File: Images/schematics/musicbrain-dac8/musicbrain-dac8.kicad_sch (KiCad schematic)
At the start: 25 parts, among them J1 BUS, J2 CV OUT, U1 AD5754BREZ, U2 AD5754BREZ, U3 ADR421

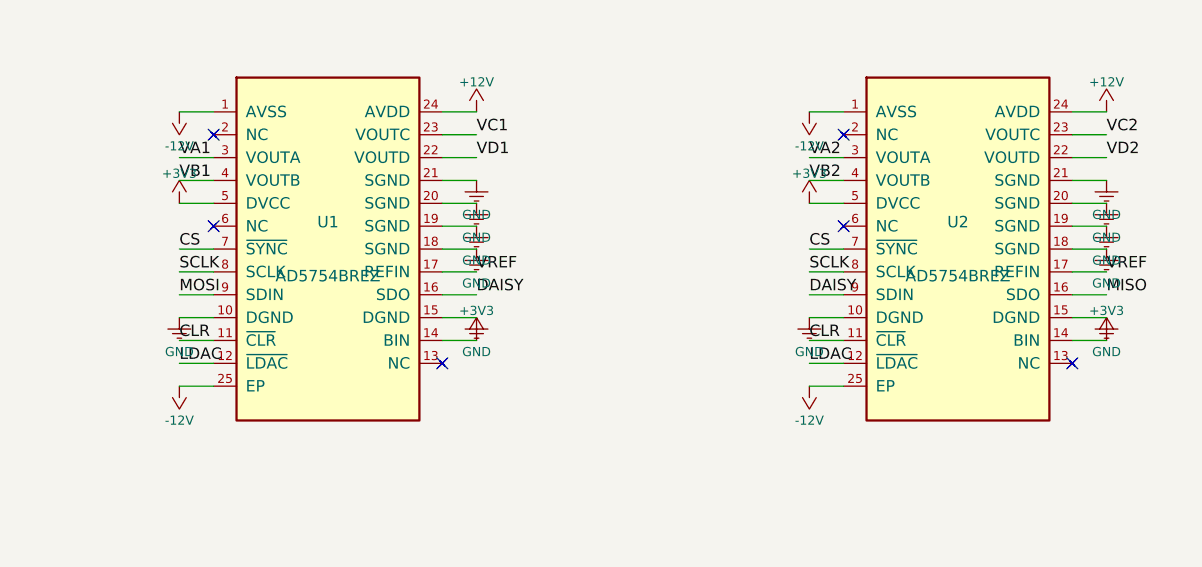
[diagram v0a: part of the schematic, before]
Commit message: DAC8-fix: correcte AD5754-pinout (~LDAC op pin 10, niet 12)
Bij het opzetten van de v2.1-check bleek de "zwevende LDAC" NIET in de
AD5754-breakout te zitten (die matcht Nick's bewezen ontwerp: pin 10 =
~LDAC, al aan GND; pin 12/13 = NC) maar in de deze sessie nieuw gemaakte
DAC8: daar was de AD5754-pinout verhaspeld (LDAC op pin 12 = NC-pad, echte
pin 10 aan GND). Gevolg: de bus-LDAC deed niets en de DAC updatete
transparant i.p.v. sample-synchroon.

- symbool + netmap gecorrigeerd tegen Nick's pinout: 5=BIN(+3V3),
  10=~LDAC(bus), 11=~CLR, 12/13=NC, 14=DVCC(+3V3), 15=DGND(GND)
- LDAC opnieuw geroute naar pin 10 via een trap-entry (CLR 0,6mm
  opgeschoven om ruimte te maken); U2-tak op F.Cu om de CS-B-hop te mijden
- ERC 0, netlijst pad-voor-pad geverifieerd, DRC 0/0; PDF's + fab herzien

De AD5754-breakout blijft ongewijzigd (was al correct).

Co-Authored-By: Claude Fable 5 <noreply@anthropic.com>
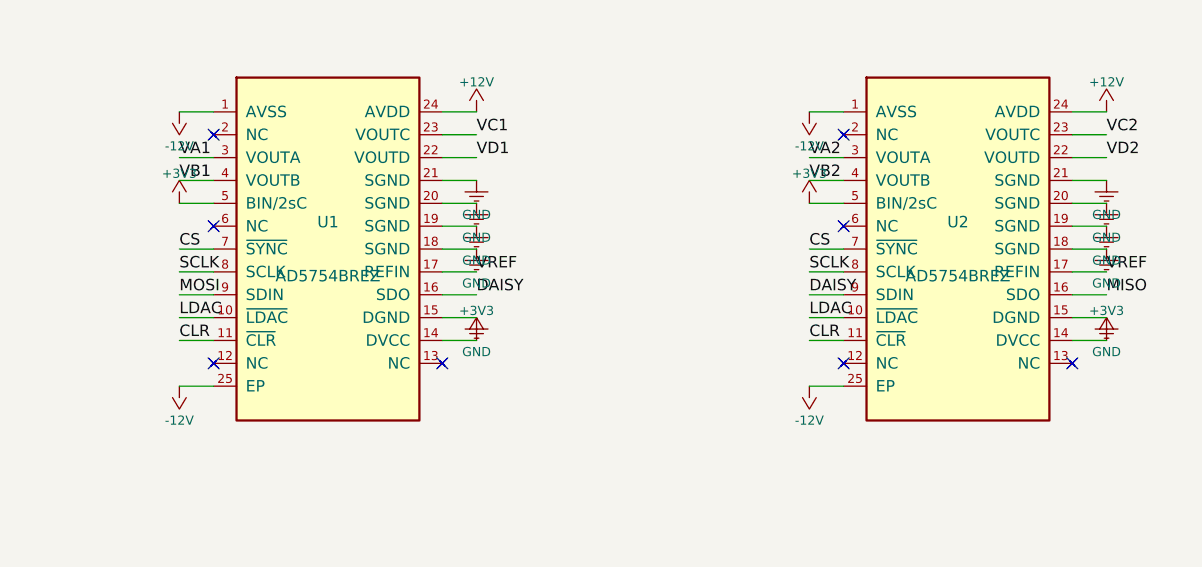
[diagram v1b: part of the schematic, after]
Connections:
- net GND: no longer U1.10 (DGND), U2.10 (DGND)
- net LDAC: now also U1.10 (~{LDAC}), U2.10 (~{LDAC}); no longer U1.12 (~{LDAC}), U2.12 (~{LDAC})
- no-connect marks 11 -> 13

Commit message: DAC8: 10uF bulk op VREF (ADR421-ontkoppeling per datasheet)
Cross-check tegen doc/data-sheets/AD5754BREZ data.md bevestigde de pinout
(3 bronnen) en dat de referentiepen 0,1uF + 10uF hoort te krijgen. C6 was
er al (0,1uF); C14 (10uF, oostrand tussen +12V-spine en C1) toegevoegd op
/VREF naast C6, U1.17, U2.17, U3.8. ERC 0, netcheck OK, DRC 0/0; PDF's +
fab herzien. README: BREZ heeft geen interne ref -> ADR421 verplicht.

Co-Authored-By: Claude Fable 5 <noreply@anthropic.com>
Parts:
- added C14: 10u, Capacitor_SMD:CP_Elec_4x5.3, symbol Device:C_Polarized
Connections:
- net GND: now also C14.2 (-)
- net VREF: now also C14.1 (+)
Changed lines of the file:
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@@
     (instances (project "musicbrain-dac8" (path "/d0900000-0000-4000-8000-000000000000" (reference "#PWR056") (unit 1))))
+  )
+  (symbol (lib_id "Device:C_Polarized") (at 266 190 0)
+    (unit 1) (exclude_from_sim no) (in_bom yes) (on_board yes) (dnp no)
+    (property "Reference" "C14" (at 266 187 0) (effects (font (size 1.27 1.27))))
+    (property "Value" "10u" (at 266 193 0) (effects (font (size 1.27 1.27))))
+    (property "Footprint" "Capacitor_SMD:CP_Elec_4x5.3" (at 266 190 0) (effects (font (size 1.27 1.27)) (hide yes)))
+    (property "Datasheet" "" (at 266 190 0) (effects (font (size 1.27 1.27)) (hide yes)))
+    (instances (project "musicbrain-dac8" (path "/d0900000-0000-4000-8000-000000000000" (reference "C14") (unit 1))))
+  )
+  (wire (pts (xy 266 186.19) (xy 266 184.5)) (stroke (width 0) (type default)))
+  (label "VREF" (at 266 184.5 0) (effects (font (size 1.27 1.27)) (justify left bottom)))
+  (wire (pts (xy 266 193.81) (xy 266 196.17)) (stroke (width 0) (type default)))
+  (symbol (lib_id "power:GND") (at 266 196.17 0)
+    (unit 1) (exclude_from_sim no) (in_bom yes) (on_board yes) (dnp no)
+    (property "Reference" "#PWR057" (at 266 196.17 0) (effects (font (size 1.27 1.27)) (hide yes)))
+    (property "Value" "GND" (at 266 199.98 0) (effects (font (size 1.016 1.016))))
+    (property "Footprint" "" (at 266 196.17 0) (effects (font (size 1.27 1.27)) (hide yes)))
+    (property "Datasheet" "" (at 266 196.17 0) (effects (font (size 1.27 1.27)) (hide yes)))
+    (instances (project "musicbrain-dac8" (path "/d0900000-0000-4000-8000-000000000000" (reference "#PWR057") (unit 1))))
   )
   (wire (pts (xy 300 150) (xy 305.08 150)) (stroke (width 0) (type default)))
   (symbol (lib_id "power:+12V") (at 300 150 0)
     (unit 1) (exclude_from_sim no) (in_bom yes) (on_board yes) (dnp no)
-    (property "Reference" "#PWR057" (at 300 150 0) (effects (font (size 1.27 1.27)) (hide yes)))
+    (property "Reference" "#PWR058" (at 300 150 0) (effects (font (size 1.27 1.27)) (hide yes)))
     (property "Value" "+12V" (at 300 146.698 0) (effects (font (size 1.016 1.016))))
     (property "Footprint" "" (at 300 150 0) (effects (font (size 1.27 1.27)) (hide yes)))
     (property "Datasheet" "" (at 300 150 0) (effects (font (size 1.27 1.27)) (hide yes)))
-    (instances (project "musicbrain-dac8" (path "/d0900000-0000-4000-8000-000000000000" (reference "#PWR057") (unit 1))))
+    (instances (project "musicbrain-dac8" (path "/d0900000-0000-4000-8000-000000000000" (reference "#PWR058") (unit 1))))
   )
   (symbol (lib_id "power:PWR_FLAG") (at 305.08 150 0)
@@
   (symbol (lib_id "power:-12V") (at 314 150 0)
     (unit 1) (exclude_from_sim no) (in_bom yes) (on_board yes) (dnp no)
-    (property "Reference" "#PWR058" (at 314 150 0) (effects (font (size 1.27 1.27)) (hide yes)))
+    (property "Reference" "#PWR059" (at 314 150 0) (effects (font (size 1.27 1.27)) (hide yes)))
     (property "Value" "-12V" (at 314 153.81 0) (effects (font (size 1.016 1.016))))
     (property "Footprint" "" (at 314 150 0) (effects (font (size 1.27 1.27)) (hide yes)))
     (property "Datasheet" "" (at 314 150 0) (effects (font (size 1.27 1.27)) (hide yes)))
-    (instances (project "musicbrain-dac8" (path "/d0900000-0000-4000-8000-000000000000" (reference "#PWR058") (unit 1))))
+    (instances (project "musicbrain-dac8" (path "/d0900000-0000-4000-8000-000000000000" (reference "#PWR059") (unit 1))))
   )
   (symbol (lib_id "power:PWR_FLAG") (at 319.08 150 0)
@@
   (symbol (lib_id "power:+3V3") (at 328 150 0)
     (unit 1) (exclude_from_sim no) (in_bom yes) (on_board yes) (dnp no)
-    (property "Reference" "#PWR059" (at 328 150 0) (effects (font (size 1.27 1.27)) (hide yes)))
+    (property "Reference" "#PWR060" (at 328 150 0) (effects (font (size 1.27 1.27)) (hide yes)))
     (property "Value" "+3V3" (at 328 146.698 0) (effects (font (size 1.016 1.016))))
     (property "Footprint" "" (at 328 150 0) (effects (font (size 1.27 1.27)) (hide yes)))
     (property "Datasheet" "" (at 328 150 0) (effects (font (size 1.27 1.27)) (hide yes)))
-    (instances (project "musicbrain-dac8" (path "/d0900000-0000-4000-8000-000000000000" (reference "#PWR059") (unit 1))))
+    (instances (project "musicbrain-dac8" (path "/d0900000-0000-4000-8000-000000000000" (reference "#PWR060") (unit 1))))
   )
   (symbol (lib_id "power:PWR_FLAG") (at 333.08 150 0)
@@
   (symbol (lib_id "power:GND") (at 342 150 0)
     (unit 1) (exclude_from_sim no) (in_bom yes) (on_board yes) (dnp no)
-    (property "Reference" "#PWR060" (at 342 150 0) (effects (font (size 1.27 1.27)) (hide yes)))
+    (property "Reference" "#PWR061" (at 342 150 0) (effects (font (size 1.27 1.27)) (hide yes)))
     (property "Value" "GND" (at 342 153.81 0) (effects (font (size 1.016 1.016))))
     (property "Footprint" "" (at 342 150 0) (effects (font (size 1.27 1.27)) (hide yes)))
     (property "Datasheet" "" (at 342 150 0) (effects (font (size 1.27 1.27)) (hide yes)))
-    (instances (project "musicbrain-dac8" (path "/d0900000-0000-4000-8000-000000000000" (reference "#PWR060") (unit 1))))
+    (instances (project "musicbrain-dac8" (path "/d0900000-0000-4000-8000-000000000000" (reference "#PWR061") (unit 1))))
   )
   (symbol (lib_id "power:PWR_FLAG") (at 347.08 150 0)
